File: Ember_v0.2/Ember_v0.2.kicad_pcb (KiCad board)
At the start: 2 copper layers, 87 parts, among them J3 DROGUE, J4 BATT_CONN, J5 MAIN, J6 MAN2, J7 DROGUE2, J8 ARM, Q1 SISA96DN-T1, Q2 SISA96DN-T1, Q3 SISA96DN-T1, Q4 SISA96DN-T1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

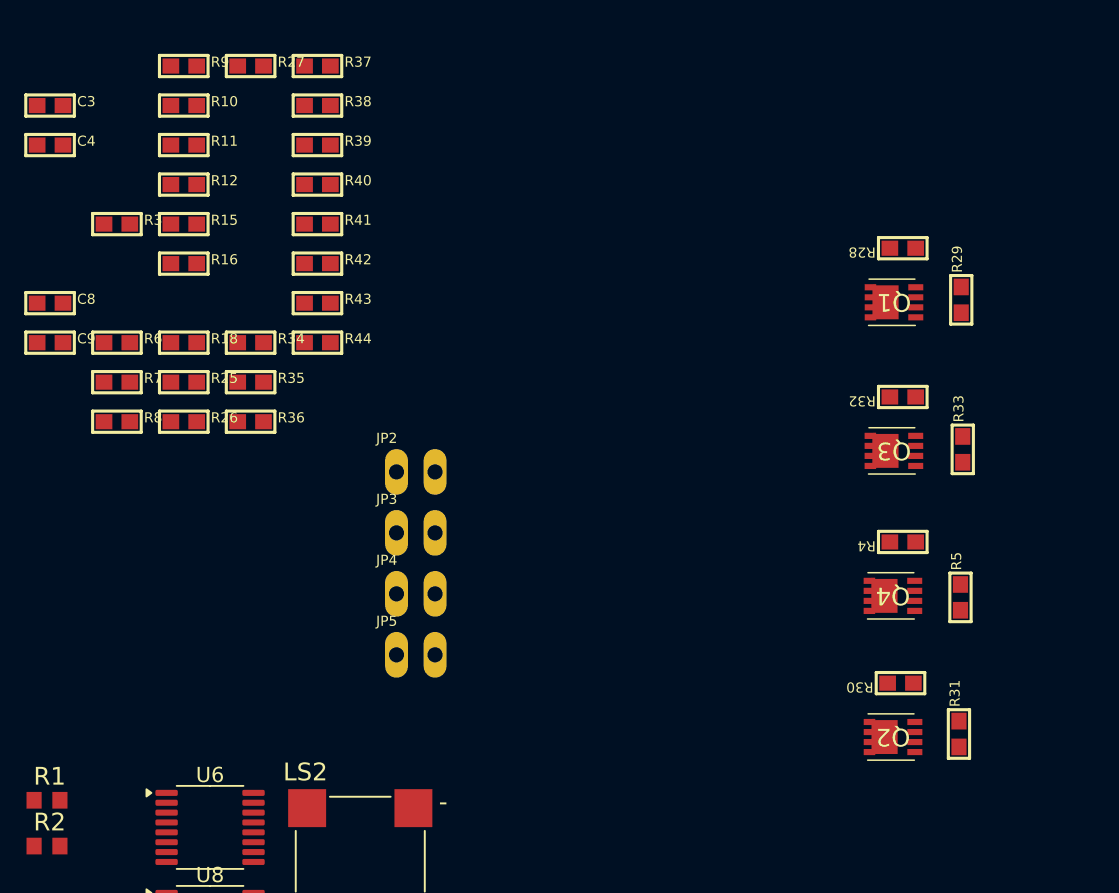
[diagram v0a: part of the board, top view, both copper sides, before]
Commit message: main board routing started
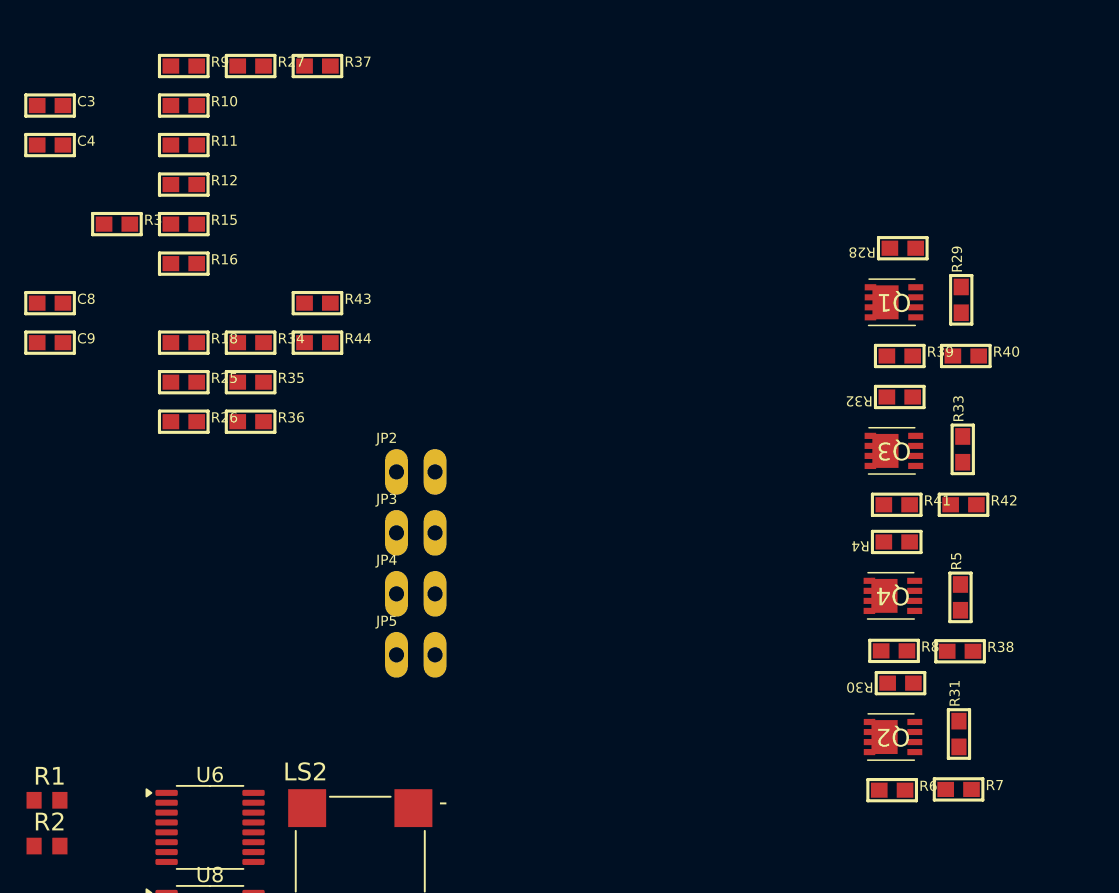
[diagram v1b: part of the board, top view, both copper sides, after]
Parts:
- moved R7 61.6 mm to (149.1, 89.8)
- moved R6 59.0 mm to (144.8, 89.8)
- moved R38 55.5 mm to (149.2, 80.7)
- moved R8 53.4 mm to (144.9, 80.7)
- moved R42 45.4 mm to (149.4, 71.0)
- moved R40 44.2 mm to (149.6, 61.2)
- moved R41 42.4 mm to (145.1, 71.0)
- moved R39 40.8 mm to (145.2, 61.2)
- moved R4 0.40 mm to (145.1, 73.5)
- moved R32 0.20 mm to (145.2, 64.0)
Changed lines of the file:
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@@
 	(footprint "microbuilder:0603"
 		(layer "F.Cu")
-		(at 145.45 73.5 180)
+		(at 145.05 73.5 180)
 		(descr "0603 (1608 Metric)")
 		(property "Reference" "R4"
@@
 	(footprint "microbuilder:0603"
 		(layer "F.Cu")
-		(at 106.8929 52.5622)
+		(at 145.05 71.05)
 		(descr "0603 (1608 Metric)")
 		(property "Reference" "R41"
@@
 	(footprint "microbuilder:0603"
 		(layer "F.Cu")
-		(at 93.6833 65.5782)
+		(at 144.875 80.675)
 		(descr "0603 (1608 Metric)")
 		(property "Reference" "R8"
@@
 	(footprint "microbuilder:0603"
 		(layer "F.Cu")
-		(at 145.45 63.95 180)
+		(at 145.25 63.95 180)
 		(descr "0603 (1608 Metric)")
 		(property "Reference" "R32"
@@
 	(footprint "microbuilder:0603"
 		(layer "F.Cu")
-		(at 106.8929 49.959)
+		(at 149.6 61.25)
 		(descr "0603 (1608 Metric)")
 		(property "Reference" "R40"
@@
 	(footprint "microbuilder:0603"
 		(layer "F.Cu")
-		(at 106.8929 44.7526)
+		(at 149.225 80.7)
 		(descr "0603 (1608 Metric)")
 		(property "Reference" "R38"
@@
 	(footprint "microbuilder:0603"
 		(layer "F.Cu")
-		(at 106.8929 47.3558)
+		(at 145.25 61.25)
 		(descr "0603 (1608 Metric)")
 		(property "Reference" "R39"
@@
 	(footprint "microbuilder:0603"
 		(layer "F.Cu")
-		(at 93.6833 60.3718)
+		(at 144.75 89.85)
 		(descr "0603 (1608 Metric)")
 		(property "Reference" "R6"
@@
 	(footprint "microbuilder:0603"
 		(layer "F.Cu")
-		(at 93.6833 62.975)
+		(at 149.125 89.8)
 		(descr "0603 (1608 Metric)")
 		(property "Reference" "R7"
@@
 	(footprint "microbuilder:0603"
 		(layer "F.Cu")
-		(at 106.8929 55.1654)
+		(at 149.45 71.05)
 		(descr "0603 (1608 Metric)")
 		(property "Reference" "R42"

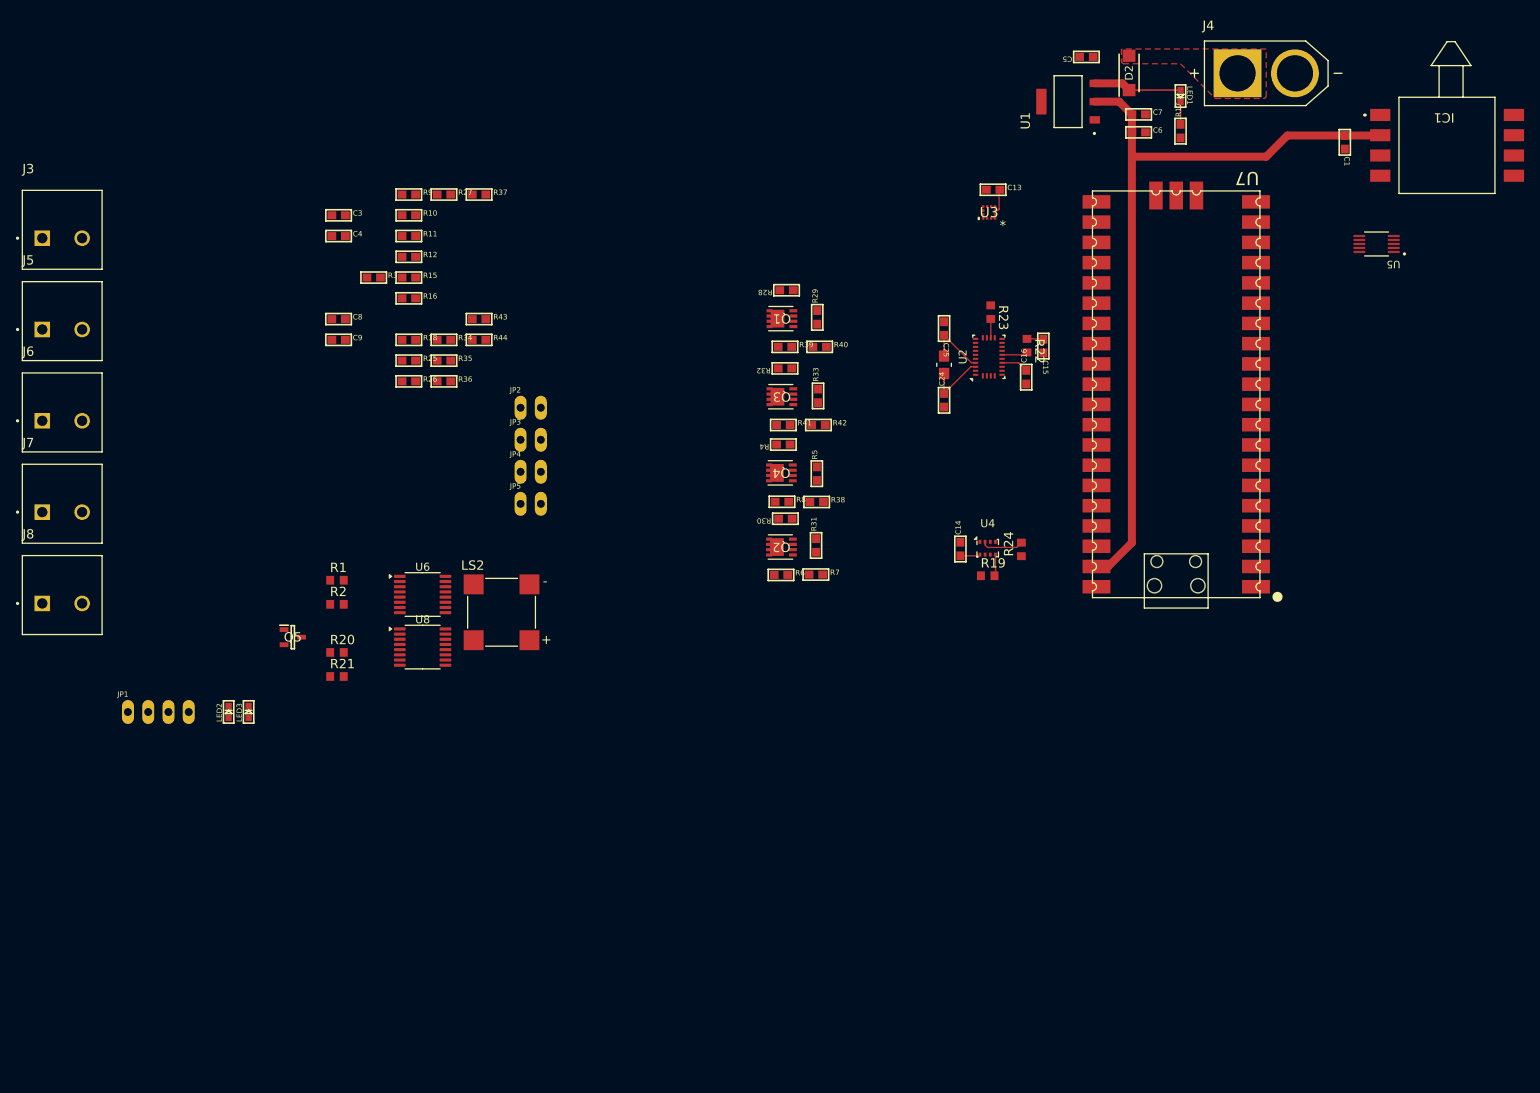
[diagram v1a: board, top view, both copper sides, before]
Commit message: Some corrections done and main board routing halfway done
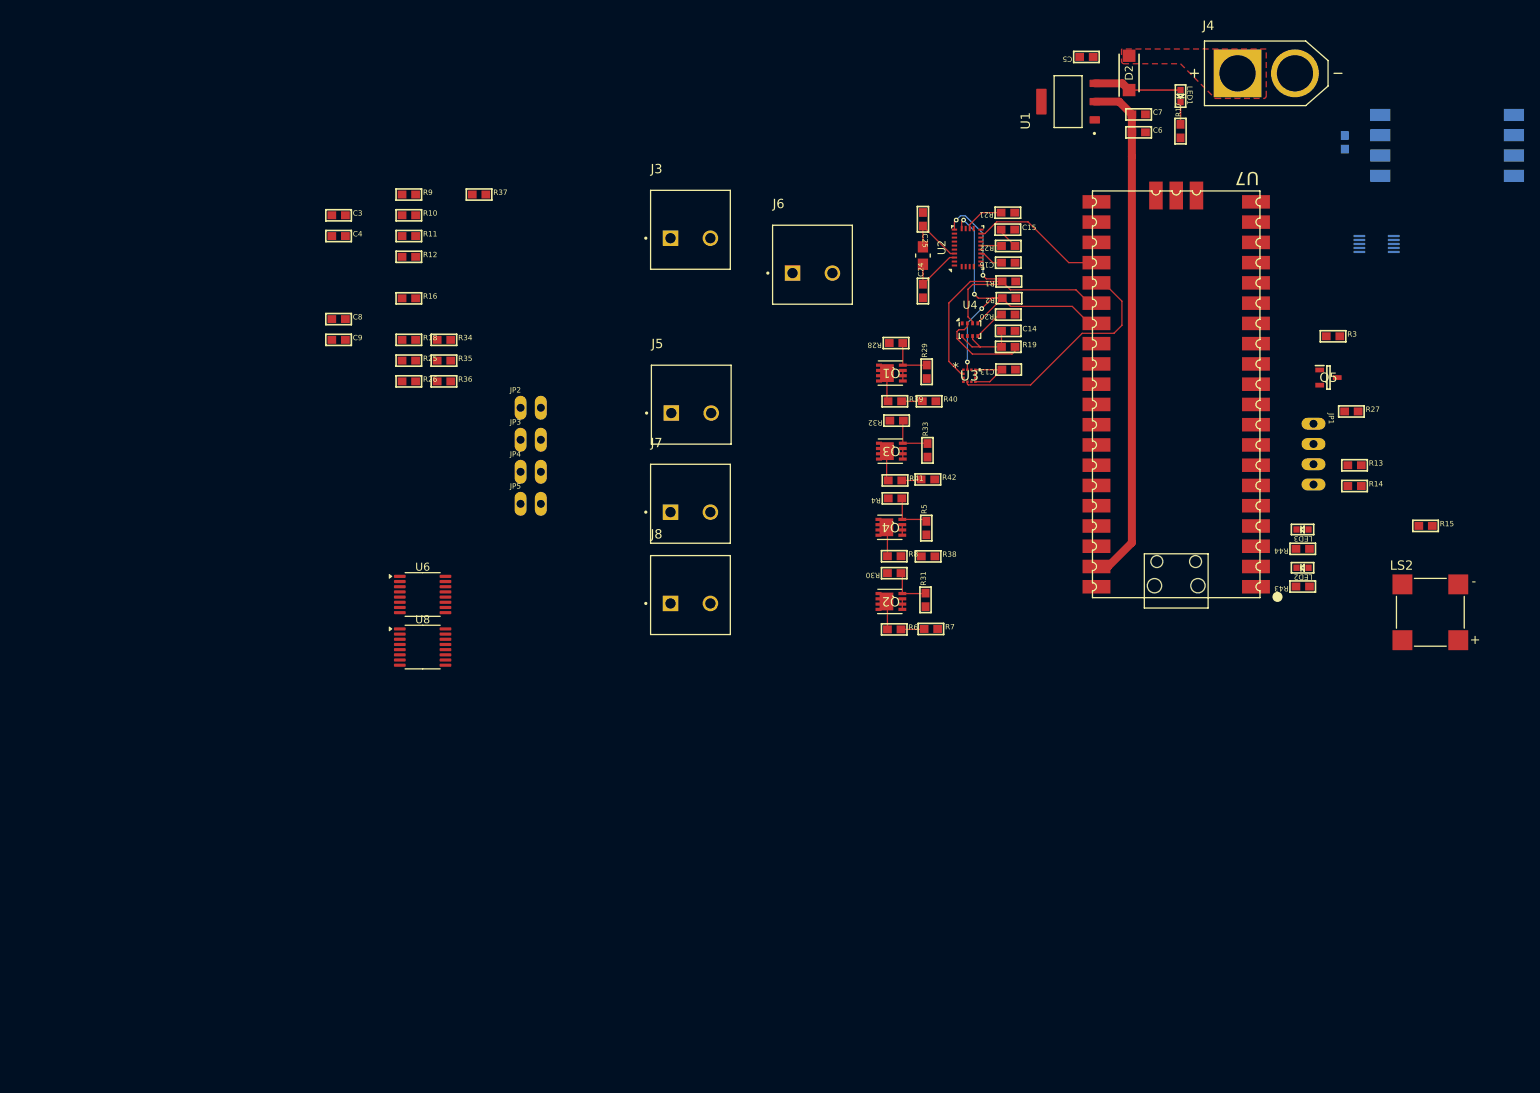
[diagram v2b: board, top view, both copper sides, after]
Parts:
- removed R23, R24: 10k ohm, adafruit:R0603
- added R13: 10k, microbuilder:0603, F.Cu at (216.7, 76.1)
- added R14: 10k, microbuilder:0603, F.Cu at (216.7, 78.7)
- C1, IC1, U5: moved to B.Cu
- R1, R19, R2, R20, R21, R22: value 10k ohm -> 10k; footprint adafruit:R0603 -> microbuilder:0603
- moved JP1 148.4 mm to (211.5, 74.7), turned to -90 degrees
- moved LED2 135.9 mm to (210.2, 89.0), turned to 90 degrees
- moved LED3 134.1 mm to (210.2, 84.2), turned to 90 degrees
- moved Q5 133.9 mm to (213.4, 65.1)
- moved R15 131.2 mm to (225.6, 83.7)
- moved R3 120.5 mm to (214.0, 59.9)
- moved R27 117.0 mm to (216.3, 69.3)
- moved LS2 116.5 mm to (226.2, 94.5)
- moved R43 108.6 mm to (210.2, 91.3), turned to 180 degrees
- moved R44 106.6 mm to (210.2, 86.6), turned to 180 degrees
- moved R21 102.3 mm to (173.2, 44.4), turned to 180 degrees
- moved J6 95.9 mm to (148.7, 52.0)
- moved R20 94.2 mm to (173.2, 57.2), turned to 180 degrees
- moved R2 92.6 mm to (173.3, 55.1), turned to 180 degrees
- moved R1 92.2 mm to (173.3, 53.0), turned to 180 degrees
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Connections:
- JP1 pad 1: /5v -> /V_BATT
- R1 pad 2: /B2B_RX -> /SDA
- R19 pad 1: /GND -> /3v3
- R19 pad 2: Net-(U4-SDO) -> Net-(U4-CSB)
- R2 pad 2: /B2B_TX -> /SCL
- R20 pad 1: /3v3 -> /GND
- R20 pad 2: /SDA -> Net-(U4-SDO)
- R21 pad 1: /3v3 -> /GND
- R21 pad 2: /SCL -> Net-(U2-COM3)
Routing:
- net /SDA: track 0.00 -> 53.5 mm, vias 0 -> 2
- net /SCL: track 0.00 -> 43.8 mm, vias 0 -> 4
- net /5v: track 97.0 -> 64.7 mm
- net /KX_INT: track 0.00 -> 30.0 mm
- net /BNO_INT: track 0.00 -> 17.2 mm
- net /3v3: track 7.62 -> 19.4 mm
- net Net-(U4-CSB): track 5.32 -> 11.6 mm
- net /G_MAIN: track 0.00 -> 5.98 mm
- net /G_MAIN2: track 0.00 -> 5.78 mm
- net Net-(Q4-G): track 0.00 -> 5.78 mm
- net /G_DROGUE: track 0.00 -> 5.56 mm
- net /GND: track 0.00 -> 5.28 mm
- net /PYRO_MAIN: track 0.00 -> 3.69 mm
- net /PYRO_DROGUE2: track 0.00 -> 3.68 mm
- net /PYRO_MAIN2: track 0.00 -> 3.59 mm
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
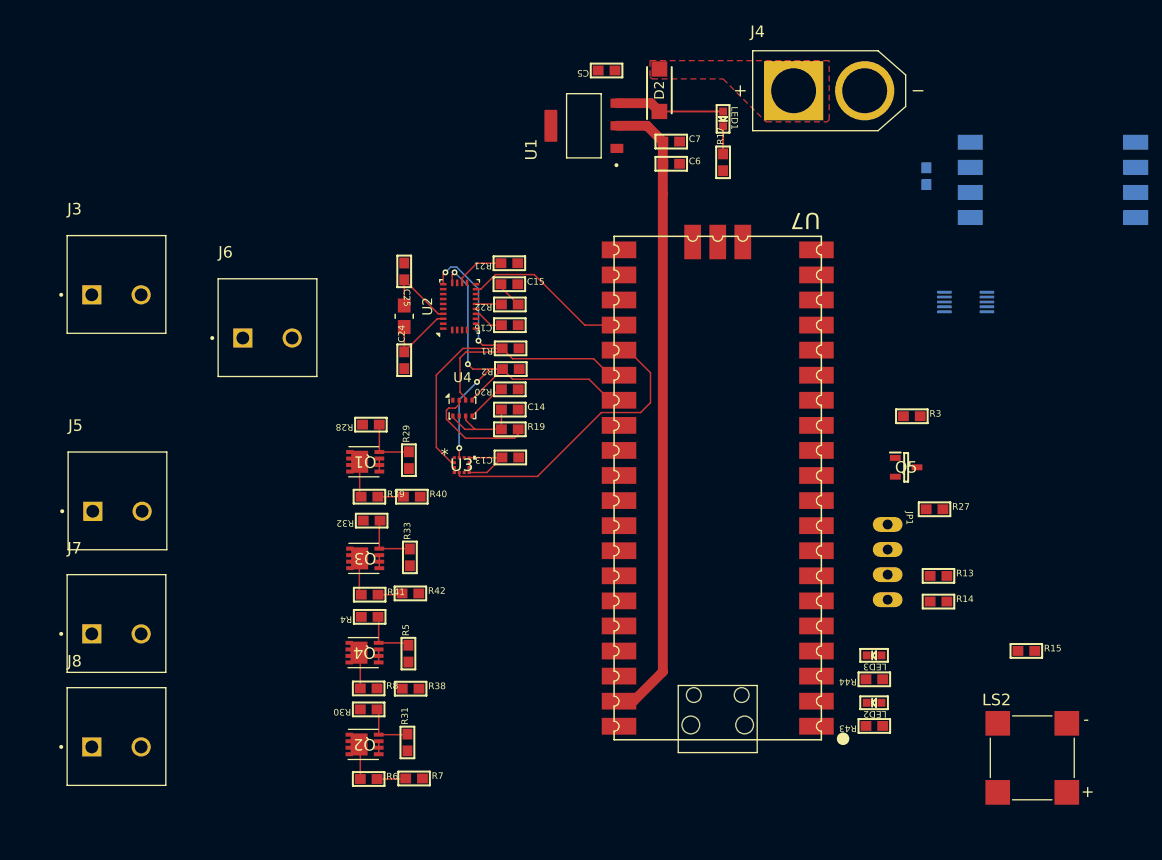
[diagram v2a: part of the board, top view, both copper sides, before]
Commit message: Some changes on V0.2 layout
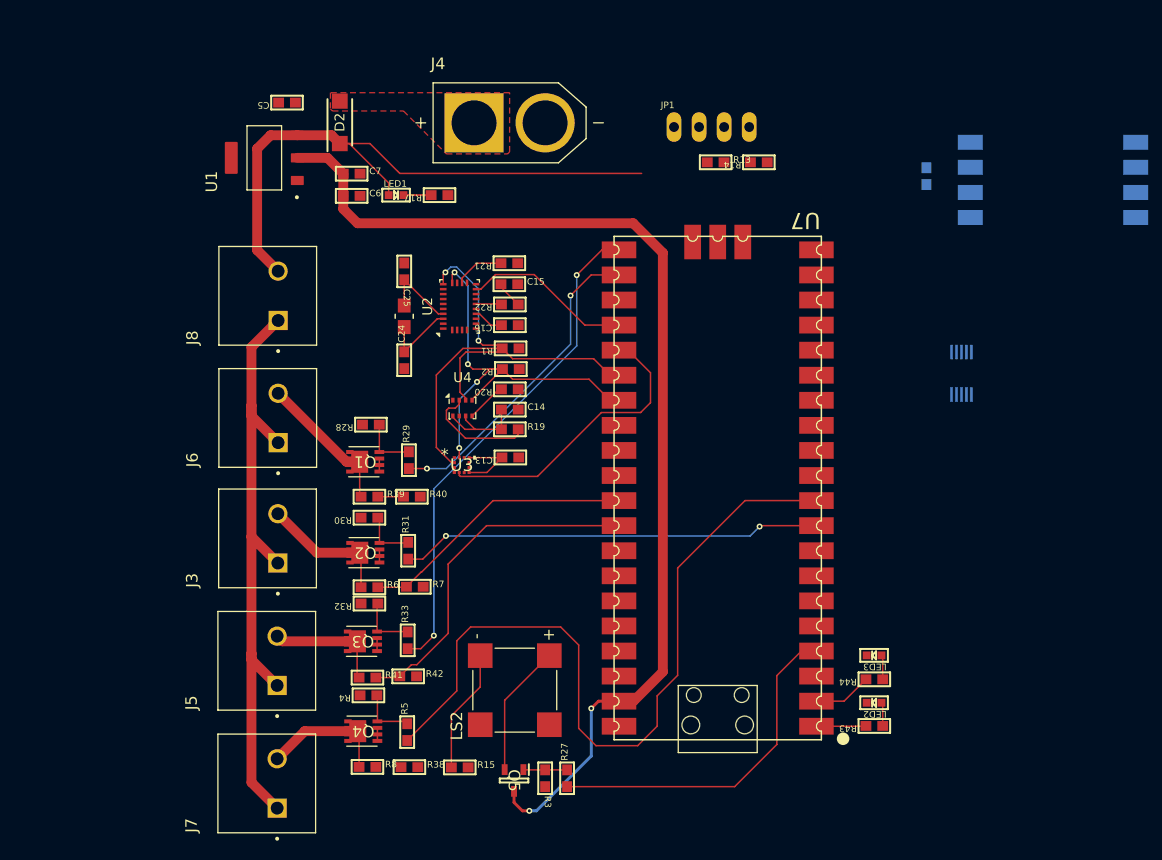
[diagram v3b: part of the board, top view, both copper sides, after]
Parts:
- moved R15 58.6 mm to (168.2, 95.5)
- moved LS2 52.9 mm to (173.8, 87.7), turned to 90 degrees
- moved R3 52.2 mm to (176.8, 96.6), turned to -90 degrees
- moved Q5 50.8 mm to (173.7, 96.8), turned to -90 degrees
- moved J8 48.5 mm to (149.8, 47.7), turned to 90 degrees
- moved R14 48.1 mm to (198.5, 34.2), turned to 180 degrees
- moved R13 47.6 mm to (194.1, 34.2)
- moved JP1 47.5 mm to (193.7, 30.6), turned to 0 degrees
- moved R27 46.1 mm to (179.1, 96.6), turned to 90 degrees
- moved LED1 34.0 mm to (161.7, 37.5), turned to -90 degrees
- moved C5 32.5 mm to (150.7, 28.1)
- moved C6 32.5 mm to (157.2, 37.6)
- moved C7 32.5 mm to (157.2, 35.4)
- moved D2 32.5 mm to (156.0, 30.1)
- moved J4 32.5 mm to (173.2, 30.2)
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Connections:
- Q5 pad 3: /3v3 -> /5v
- R39 pad 2: Net-(U7-GP27) -> Net-(U5-AIN2)
- R40 pad 1: Net-(U7-GP27) -> Net-(U5-AIN2)
- R41 pad 2: Net-(U7-GP26) -> Net-(U7-GP27)
- R42 pad 1: Net-(U7-GP26) -> Net-(U7-GP27)
- R6 pad 2: Net-(U5-AIN2) -> Net-(U7-GP26)
- R7 pad 1: Net-(U5-AIN2) -> Net-(U7-GP26)
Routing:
- net /DROGUE2: track 0.00 -> 77.6 mm
- net /VCC_PYRO: track 0.00 -> 64.6 mm
- net /V_BATT: track 11.1 -> 62.2 mm
- net /MAIN: track 0.00 -> 51.1 mm, vias 0 -> 2
- net /5v: track 64.7 -> 110.8 mm, vias 0 -> 2
- net /DROGUE: track 0.00 -> 42.8 mm, vias 0 -> 2
- net /BUZZER: track 0.00 -> 35.0 mm
- net Net-(U7-GP27): track 2.60 -> 35.3 mm
- net /MAIN2: track 0.00 -> 32.3 mm, vias 0 -> 2
- net Net-(U7-GP26): track 2.68 -> 28.1 mm
- net Net-(Q5-S): track 0.00 -> 13.4 mm
- net Net-(LS2-PadN): track 0.00 -> 12.5 mm
- net /PYRO_MAIN2: track 3.59 -> 14.7 mm
- net /PYRO_DROGUE: track 3.55 -> 13.5 mm
- net /PYRO_DROGUE2: track 3.68 -> 13.0 mm
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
